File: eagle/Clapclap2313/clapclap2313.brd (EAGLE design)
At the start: 50 x 50 mm, 24 parts, among them K1 4052, M1 Mic

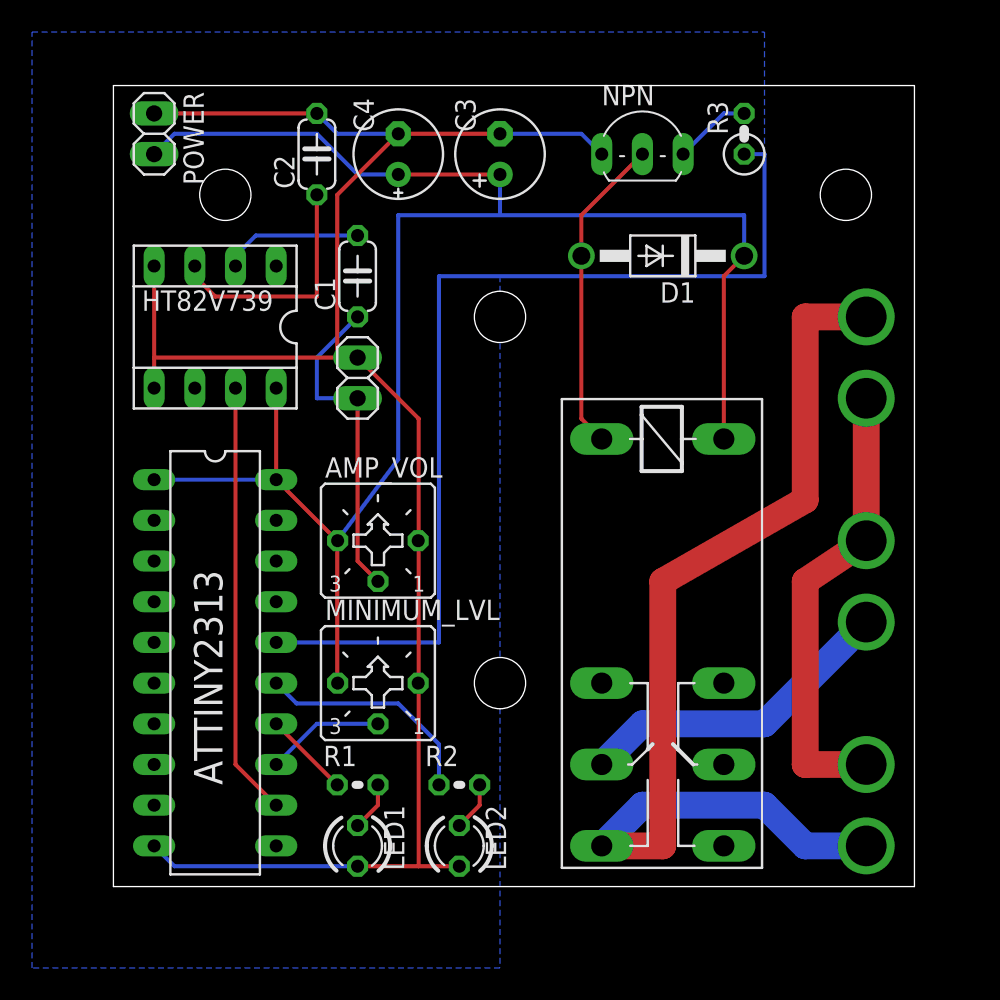
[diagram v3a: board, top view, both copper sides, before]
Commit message: Added ECB indication for the transistor
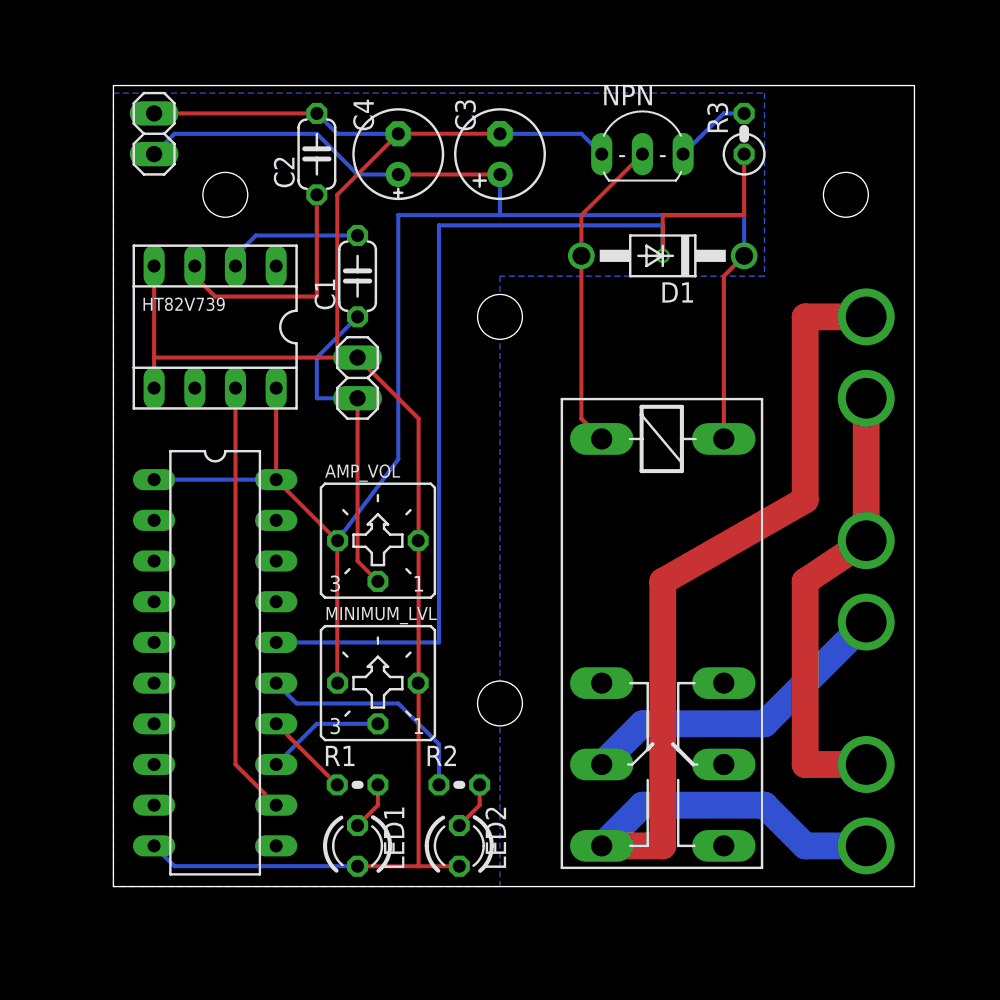
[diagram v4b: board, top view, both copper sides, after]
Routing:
- net N$2: track 62.2 -> 63.5 mm, vias 0 -> 1
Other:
- board text added: "+5v"
- board text added: "44200"
- board text added: "ATTINY2313"
- board text added: "Clapclap 2313"
- board text added: "E C B"
- board text added: "GND"
- board text added: "Order#"
- board text added: "http://kalshagar.wikispaces.com/Clapclap+2313"
- board text added: "v1.2 - Feb2012"
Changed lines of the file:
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@@
 <?xml version="1.0" encoding="utf-8"?>
 <!DOCTYPE eagle SYSTEM "eagle.dtd">
-<eagle version="6.0">
+<eagle version="6.3">
 <drawing>
 <settings>
@@
 <wire x1="50" y1="50" x2="0" y2="50" width="0" layer="20"/>
 <wire x1="0" y1="50" x2="0" y2="0" width="0" layer="20"/>
-<hole x="6.985" y="43.18" drill="3.2"/>
-<hole x="45.72" y="43.18" drill="3.2"/>
-<hole x="24.13" y="12.7" drill="3.2"/>
-<hole x="24.13" y="35.56" drill="3.2"/>
+<hole x="6.985" y="43.18" drill="2.8"/>
+<hole x="45.72" y="43.18" drill="2.8"/>
+<hole x="24.13" y="11.43" drill="2.8"/>
+<hole x="24.13" y="35.56" drill="2.8"/>
 <rectangle x1="45.085" y1="0" x2="50.165" y2="9.525" layer="48"/>
 <rectangle x1="45.085" y1="27.94" x2="50.165" y2="38.1" layer="48"/>
-<wire x1="41.275" y1="49.53" x2="41.275" y2="32.385" width="0.4064" layer="48" style="shortdash"/>
-<wire x1="41.275" y1="32.385" x2="26.67" y2="32.385" width="0.4064" layer="48" style="shortdash"/>
-<wire x1="26.67" y1="32.385" x2="26.67" y2="1.27" width="0.4064" layer="48" style="shortdash"/>
+<wire x1="41.275" y1="40.64" x2="41.275" y2="32.385" width="0.4064" layer="48" style="shortdash"/>
+<wire x1="41.275" y1="32.385" x2="27.305" y2="32.385" width="0.4064" layer="48" style="shortdash"/>
+<wire x1="27.305" y1="32.385" x2="27.305" y2="1.27" width="0.4064" layer="48" style="shortdash"/>
 <text x="13.335" y="29.21" size="1.27" layer="48" rot="R90">Micro</text>
 <text x="17.78" y="33.02" size="1.27" layer="48" rot="R90">-</text>
@@
 <text x="49.53" y="10.16" size="1.27" layer="48" rot="R90">N</text>
 <text x="44.45" y="2.54" size="1.27" layer="48" rot="R90">Input</text>
+<text x="26.67" y="1.905" size="0.8128" layer="48" rot="R90">http://kalshagar.wikispaces.com/Clapclap+2313</text>
+<text x="22.86" y="16.51" size="1.27" layer="48" rot="R90">Clapclap 2313</text>
+<text x="24.765" y="19.05" size="0.8128" layer="48" rot="R90">v1.2 - Feb2012</text>
+<text x="13.97" y="0" size="0.8128" layer="48">-</text>
+<text x="20.32" y="0" size="0.8128" layer="48">-</text>
+<text x="13.97" y="4.445" size="0.8128" layer="48">+</text>
+<text x="20.32" y="4.445" size="0.8128" layer="48">+</text>
+<wire x1="34.29" y1="24.13" x2="34.29" y2="17.78" width="0.8128" layer="48"/>
+<wire x1="34.29" y1="17.78" x2="34.29" y2="13.97" width="0.8128" layer="48"/>
+<wire x1="34.29" y1="13.97" x2="38.1" y2="21.59" width="0.8128" layer="48"/>
+<wire x1="34.29" y1="24.13" x2="30.48" y2="17.78" width="0.8128" layer="48"/>
+<wire x1="31.75" y1="17.78" x2="34.29" y2="17.78" width="0.8128" layer="48"/>
+<wire x1="41.275" y1="40.64" x2="49.53" y2="40.64" width="0.4064" layer="48" style="shortdash"/>
+<text x="43.18" y="48.26" size="1.27" layer="48">Order#</text>
+<text x="43.815" y="46.355" size="1.27" layer="48">44200</text>
+<text x="6.985" y="3.81" size="1.27" layer="48" rot="R90">ATTINY2313</text>
+<text x="4.445" y="45.085" size="1.016" layer="48">+5v</text>
+<text x="4.445" y="47.625" size="1.016" layer="48">GND</text>
+<text x="30.48" y="42.545" size="1.27" layer="48">E C B</text>
 </plain>
 <attributes>
@@
 </class>
 </classes>
-<designrules>
+<designrules name="default">
 <description language="de">&lt;b&gt;EAGLE Design Rules&lt;/b&gt;
 &lt;p&gt;
@@
 <attribute name="MF" value="" x="0" y="-12.7" size="1.778" layer="27" rot="R270" display="off"/>
 <attribute name="OC_FARNELL" value="unknown" x="0" y="-12.7" size="1.778" layer="27" rot="R270" display="off"/>
-<attribute name="NAME" x="6.8072" y="6.35" size="1.778" layer="25" ratio="10" rot="R90"/>
 <attribute name="VALUE" x="5.588" y="24.13" size="1.778" layer="27" ratio="10" rot="R270"/>
 </element>
 <element name="HT82V739" library="ic-package" package="SOCKET-08" value="" x="6.35" y="34.925" smashed="yes" rot="R180">
 <attribute name="VALUE" x="9.398" y="35.433" size="1.27" layer="27" ratio="10" rot="R180"/>
-<attribute name="NAME" x="1.778" y="35.941" size="1.27" layer="25" ratio="10"/>
+<attribute name="NAME" x="1.778" y="35.941" size="0.8128" layer="25" ratio="10"/>
 </element>
 <element name="M1" library="pinhead" package="1X02" value="Mic" x="15.24" y="31.75" smashed="yes" rot="R90">
@@
 <attribute name="VALUE" x="29.21" y="22.352" size="1.778" layer="27" ratio="10"/>
 </element>
-<element name="MINIMUM_LVL" library="pot" package="CT6" value="5k" x="16.51" y="12.7"/>
-<element name="AMP_VOL" library="pot" package="CT6" value="5k" x="16.51" y="21.59"/>
+<element name="MINIMUM_LVL" library="pot" package="CT6" value="5k" x="16.51" y="12.7" smashed="yes">
+<attribute name="NAME" x="13.208" y="16.637" size="0.8128" layer="25" ratio="10"/>
+<attribute name="VALUE" x="13.2334" y="7.493" size="1.27" layer="27" ratio="10"/>
+</element>
+<element name="AMP_VOL" library="pot" package="CT6" value="5k" x="16.51" y="21.59" smashed="yes">
+<attribute name="NAME" x="13.208" y="25.527" size="0.8128" layer="25" ratio="10"/>
+<attribute name="VALUE" x="13.2334" y="16.383" size="1.27" layer="27" ratio="10"/>
+</element>
 <element name="POWER" library="pinhead" package="1X02" value="5v" x="2.54" y="46.99" smashed="yes" rot="R90">
-<attribute name="NAME" x="4.3688" y="49.6062" size="1.27" layer="25" ratio="10" rot="R270"/>
 <attribute name="VALUE" x="5.715" y="44.45" size="1.27" layer="27" rot="R90"/>
 </element>
@@
 <wire x1="13.97" y1="33.02" x2="15.24" y2="33.02" width="0.254" layer="1"/>
 <polygon width="0.4064" layer="16">
-<vertex x="-5.08" y="53.34"/>
-<vertex x="40.64" y="53.34"/>
+<vertex x="0" y="49.53"/>
+<vertex x="40.64" y="49.53"/>
 <vertex x="40.64" y="38.1"/>
 <vertex x="24.13" y="38.1"/>
-<vertex x="24.13" y="-5.08"/>
-<vertex x="-5.08" y="-5.08"/>
+<vertex x="24.13" y="0"/>
+<vertex x="0" y="0"/>
 </polygon>
 </signal>
@@
 <contactref element="ATTINY2313" pad="16"/>
 <contactref element="R3" pad="1"/>
-<wire x1="20.32" y1="38.1" x2="20.32" y2="15.24" width="0.254" layer="16"/>
+<wire x1="20.32" y1="40.64" x2="20.32" y2="15.24" width="0.254" layer="16"/>
 <wire x1="20.32" y1="15.24" x2="10.16" y2="15.24" width="0.254" layer="16"/>
-<wire x1="40.64" y1="38.1" x2="20.32" y2="38.1" width="0.254" layer="16"/>
-<wire x1="40.64" y1="45.72" x2="40.64" y2="38.1" width="0.254" layer="16"/>
-<wire x1="39.37" y1="45.72" x2="40.64" y2="45.72" width="0.254" layer="16"/>
+<wire x1="39.37" y1="45.72" x2="39.37" y2="41.91" width="0.254" layer="1"/>
+<wire x1="39.37" y1="41.91" x2="34.29" y2="41.91" width="0.254" layer="1"/>
+<via x="34.29" y="39.37" extent="1-16" drill="0.6"/>
+<wire x1="34.29" y1="41.91" x2="34.29" y2="39.37" width="0.254" layer="1"/>
+<wire x1="34.29" y1="39.37" x2="34.29" y2="41.275" width="0.254" layer="16"/>
+<wire x1="34.29" y1="41.275" x2="20.32" y2="41.275" width="0.254" layer="16"/>
+<wire x1="20.32" y1="41.275" x2="20.32" y2="40.64" width="0.254" layer="16"/>
 </signal>
 <signal name="N$4">
